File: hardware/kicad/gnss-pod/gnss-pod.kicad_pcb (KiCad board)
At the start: 2 copper layers, 50 x 72 mm, 75 parts, among them J1 TYPE-C-31-M-12, J2 B2B-PH-K-S(LF)(SN), J3 DNP 1x8 spare pads, SW1 TS-1187A-B-A-B BOOT, SW2 TS-1187A-B-A-B RESET, SW3 SS-12D00-G3 POWER, U1 ESP32-S3-MINI-1-N8, U2 SAM-M10Q-00B, U3 LSM6DSV16XTR, U4 BQ24073RGTR, U5 TLV75733PDYDR, U6 XC6206P332MR-G, U7 USBLC6-2SC6

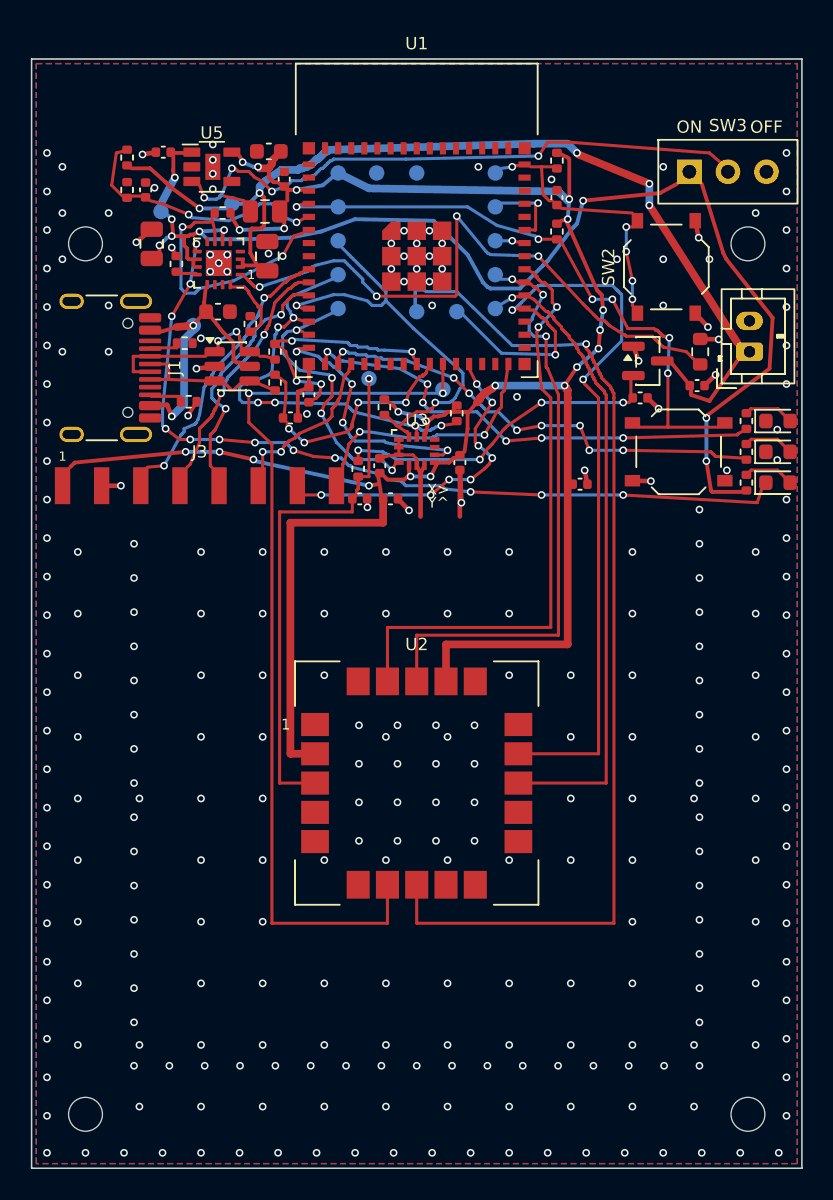
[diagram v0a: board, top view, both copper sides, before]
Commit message: GNSS pod rev A: POD-REV1 fix wave (2 HIGH + 5 MEDIUM)
- CPL exports real component centres (U1 moved 2.55 mm to its body centre).
- Charger TS senses the CELL: J2 is a 3-pin JST-PH for a pack with a 10k
  NTC; RT1 is a DNP fallback documented as not cell-temperature protected.
- u-blox >=20 mm via rule and GND-only Z1 bottom enforced as a generator
  failure; LSM6DSV16X land interior kept free of copper; USB routed as a
  top-only, via-free, 0.18 mm length-matched pair; ESP32 antenna overhangs
  the board edge (board 50 x 66.95 mm); power-budget text corrected and a
  firmware low-battery cutoff made binding; wider supply taps.
kicad-cli DRC 0/0/0; netlist self-check 263 pads.

Co-Authored-By: Claude Opus 5.5 (1M context) <noreply@anthropic.com>
Claude-Session: https://claude.ai/code/session_01FoVmPSWXi8zcJJamEeWEaQ
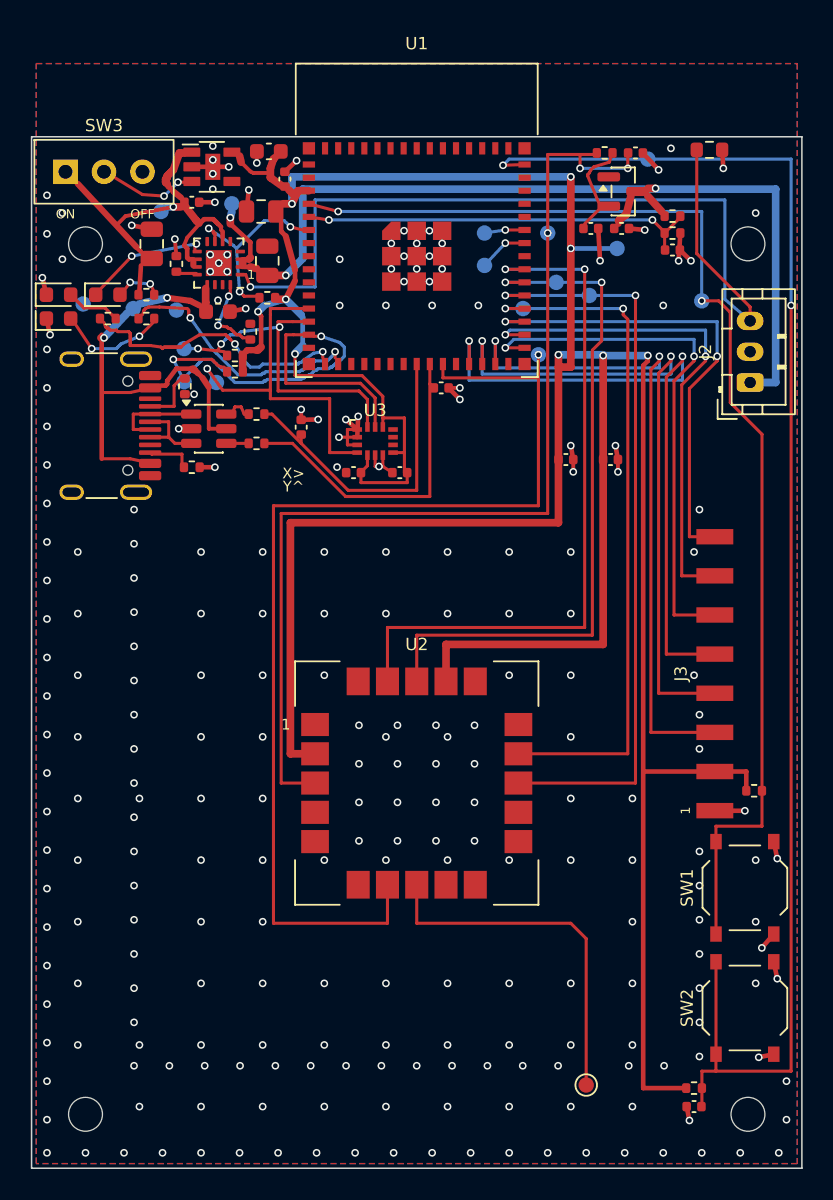
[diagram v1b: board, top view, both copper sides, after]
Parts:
- J2: value B2B-PH-K-S(LF)(SN) -> B3B-PH-K-S(LF)(SN); footprint JST_PH_B2B-PH-K_1x02_P2.00mm_Vertical -> JST_PH_B3B-PH-K_1x03_P2.00mm_Vertical
- RT1: value NCP18XH103F03RB 10k NTC -> DNP NCP18XH103F03RB 10k NTC (fallback)
- TP12: moved to F.Cu
- U7: footprint SOT-23-6 -> SOT-23-6_USBLC6-2_FlowThrough
- moved R5 60.9 mm to (43.0, 66.8), turned to 180 degrees
- moved C8 59.7 mm to (43.0, 68.0), turned to 180 degrees
- moved TP12 51.4 mm to (36.0, 66.6)
- moved SW2 48.4 mm to (46.3, 61.6)
- moved LED2 47.5 mm to (1.75, 16.9)
- moved LED1 47.4 mm to (1.75, 15.3)
- moved LED3 45.2 mm to (4.95, 15.3)
- moved R15 42.0 mm to (4.95, 16.9), turned to 0 degrees
- moved R11 40.8 mm to (7.45, 15.3), turned to 0 degrees
- moved SW3 40.5 mm to (4.70, 7.32)
- moved R16 39.9 mm to (7.45, 16.9), turned to 0 degrees
- moved R6 38.5 mm to (46.9, 47.5), turned to 180 degrees
- moved J3 35.6 mm to (44.4, 39.9), turned to 90 degrees
- moved R13 35.6 mm to (41.6, 10.2), turned to 0 degrees
- moved R14 35.5 mm to (41.6, 11.3), turned to 0 degrees
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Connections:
- J3 pad 1: 3V3 -> GND
- J3 pad 2: GND -> 3V3
- J3 pad 3: IO5 -> IO34
- J3 pad 4: IO6 -> IO33
- J3 pad 5: IO7 -> IO47
- J3 pad 6: IO14 -> IO35
- J3 pad 7: IO47 -> IO36
- J3 pad 8: IO48 -> IO37
- U1 pad 10: IO6 -> (no net)
- U1 pad 11: IO7 -> (no net)
- U1 pad 12: I2C_SDA -> IMU_INT1
- U1 pad 13: I2C_SCL -> I2C_SDA
- U1 pad 14: IMU_INT1 -> I2C_SCL
- U1 pad 15: IMU_INT2 -> (no net)
- U1 pad 18: IO14 -> (no net)
- U1 pad 28: (no net) -> IO33
- U1 pad 29: (no net) -> IO34
- U1 pad 30: IO48 -> (no net)
- U1 pad 31: (no net) -> IO35
- U1 pad 32: (no net) -> IO36
- U1 pad 33: (no net) -> IO37
- U1 pad 9: IO5 -> (no net)
- U3 pad 9: IMU_INT2 -> (no net)
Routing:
- net 3V3: track 140.1 -> 221.2 mm, vias 21 -> 9
- net EN: track 15.2 -> 94.7 mm, vias 5 -> 2
- net VSYS: track 75.2 -> 23.7 mm, vias 9 -> 1
- net CHG_N: track 53.4 -> 7.62 mm, vias 12 -> 2
- net GNSS_SAFEBOOT_N: track 67.2 -> 23.4 mm, vias 1 -> 0
- net IO34: track 0.00 -> 43.4 mm, vias 0 -> 2
- net IO33: track 0.00 -> 42.9 mm, vias 0 -> 2
- net BOOT: track 38.1 -> 77.7 mm, vias 6 -> 2
- net IO35: track 0.00 -> 34.8 mm, vias 0 -> 2
- net VBCKP: track 34.1 -> 68.3 mm, vias 1 -> 3
- net IO36: track 0.00 -> 33.1 mm, vias 0 -> 2
- net LDO_EN: track 37.8 -> 5.19 mm, vias 4 -> 2
- net IO37: track 0.00 -> 31.4 mm, vias 0 -> 2
- net IO47: track 20.3 -> 42.4 mm, vias 8 -> 2
- net TS: track 39.9 -> 58.8 mm, vias 4 -> 1
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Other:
- board size 50 x 72 mm -> 50 x 67 mm
- board text added: "BAT: + - NTC"
- board text added: "T"

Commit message: GNSS pod rev A: POD-REV2 fix wave (battery temperature, bring-up tests)
- Charging is firmware-supervised and OFF by default: R18 holds BQ24073 CE
  high; Q1 (2N7002) pulls it low only while IO37 is driven high. TS goes
  to IO6/ADC1 so firmware enables charging only inside 5-40 C (worst case
  3.6-42.4 C with a 10k B3950 pack NTC). The charger's own window is a
  backstop (worst case 1.4-51.5 C): TI SLUS810N says the TS window "cannot
  be tightened ... it can only be extended", so no resistor network can
  guarantee 45 C; a comparator is proposed for rev B.
- RT1 (PCB NTC fallback) removed.
- New spec §10A: mandatory bring-up pass/fail tests (USB enumeration +
  flashing, 3V3 during TX at USB-only and VBAT 3.5 V, measured charge stop
  points, GNSS C/N0 with WiFi on). Width-rule and SW3 pitch text corrected.
kicad-cli DRC 0/0/0; netlist self-check 268 pads.

Co-Authored-By: Claude Opus 5.5 (1M context) <noreply@anthropic.com>
Claude-Session: https://claude.ai/code/session_01FoVmPSWXi8zcJJamEeWEaQ
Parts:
- removed RT1: DNP NCP18XH103F03RB 10k NTC (fallback), R_0603_1608Metric
- added Q1: 2N7002, SOT-23, F.Cu at (43.0, 7.60)
- added R18: 100k 1%, R_0402_1005Metric, F.Cu at (14.4, 7.83)
- added R19: 10k 1%, R_0402_1005Metric, F.Cu at (45.6, 7.60)
- moved TP16 6.06 mm to (46.0, 7.35)
- moved R17 1.42 mm to (35.9, 6.55), turned to 90 degrees
- moved TP1 1.11 mm to (37.1, 12.9)
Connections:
- J3 pad 8: IO37 -> (no net)
- U1 pad 10: (no net) -> TS
- U1 pad 33: IO37 -> CHG_EN
- U4 pad 4: GND -> CHG_CE
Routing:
- net GND: track 45.5 -> 89.2 mm, vias 253 -> 254
- net CHG_CE: track 0.00 -> 33.7 mm, vias 0 -> 2
- net IO37: track 31.4 -> 0.00 mm, vias 2 -> 0
- net CHG_EN: track 0.00 -> 24.8 mm, vias 0 -> 2
- net TS: track 58.8 -> 48.4 mm, vias 1 -> 2
- net CHG_N: track 7.62 -> 11.1 mm
- net VSYS: track 23.7 -> 27.1 mm, vias 1 -> 5
- net VBCKP: track 68.3 -> 70.8 mm, vias 3 -> 1
- net EN: track 94.7 -> 92.7 mm
- net PGOOD_N: track 12.4 -> 11.2 mm
- net 3V3: track 221.2 -> 220.5 mm, vias 9 -> 12
- net VBAT: track 60.5 -> 60.7 mm, vias 3 -> 2
- net LDO_EN: track 5.19 -> 5.06 mm, vias 2 -> 0

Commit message: GNSS pod rev A: POD-REV3 fix wave (TS branch removed, test and cutoff rules)
- TS no longer reaches an ESP32 pin on rev A (no protected interface, and
  no cell to supervise): TS is on the charger and J2.3 only; IO6 NC.
  Firmware keeps CHG_EN low on rev A (charging always off); supervision
  and a protected TS interface move to rev B.
- §10A test 3 measures the charger TS thresholds with a decade box
  standing in for the NTC; no real cell is ever heated or charged outside
  its rating.
- Low-battery cutoff applies only on battery (PGOOD_N high on GPIO2), never
  on USB-only units.
- Q1 VGS(th) corrected to 1.0/1.6/2.5 V with the 3.3 V gate margin; stale
  text and the GND-fragment note fixed. __pycache__ untracked + ignored.
kicad-cli DRC 0/0/0; netlist self-check 268 pads.

Co-Authored-By: Claude Opus 5.5 (1M context) <noreply@anthropic.com>
Claude-Session: https://claude.ai/code/session_01FoVmPSWXi8zcJJamEeWEaQ
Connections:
- U1 pad 10: TS -> (no net)
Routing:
- net TS: track 48.4 -> 46.3 mm, vias 2 -> 1
